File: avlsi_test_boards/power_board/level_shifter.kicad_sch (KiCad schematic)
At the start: 7 parts, among them U19 SN74LVC16T245DLR

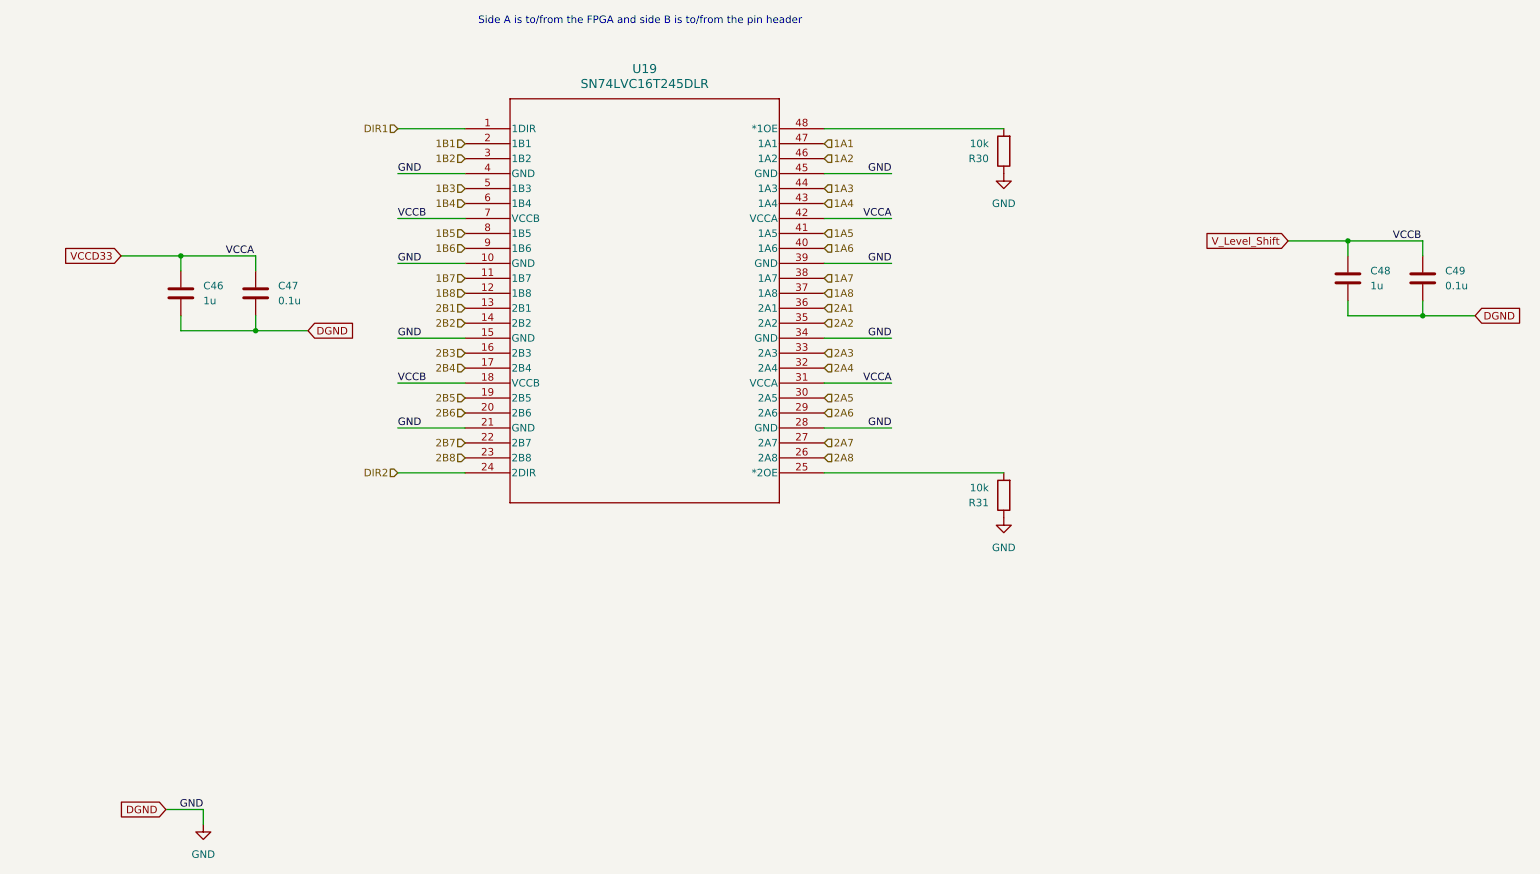
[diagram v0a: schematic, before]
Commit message: Add updated power board layout and schematic
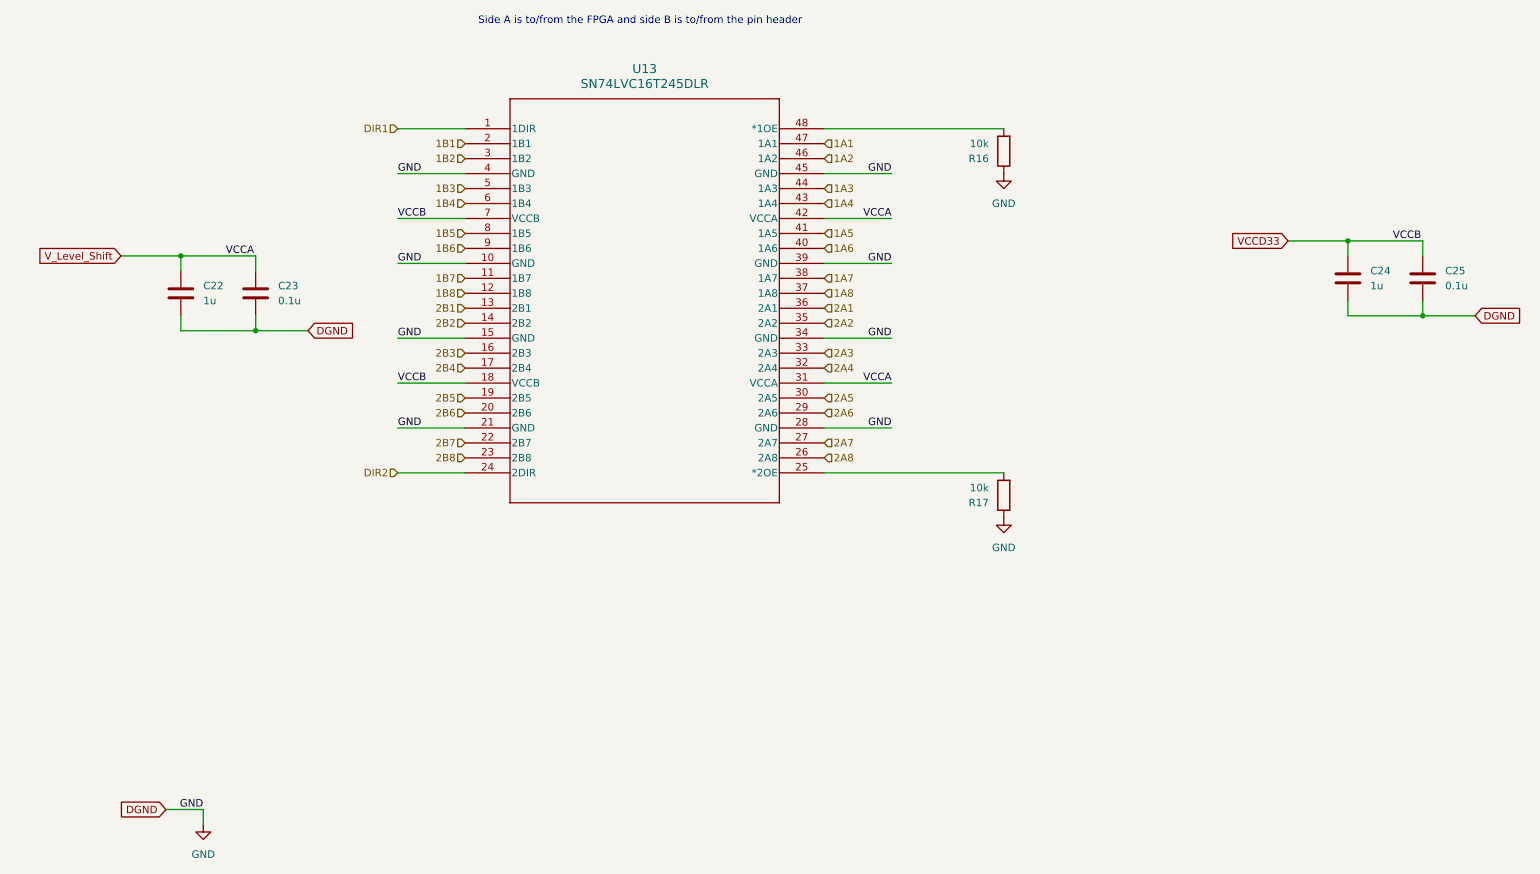
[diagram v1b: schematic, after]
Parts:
- renumbered C46 to C22, C47 to C23, C48 to C24, C49 to C25, R30 to R16, R31 to R17, U19 to U13
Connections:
- net VCCD33: now also C24.1, C25.1, U13.18 (VCCB), U13.7 (VCCB); no longer C22.1, C23.1, U13.31 (VCCA), U13.42 (VCCA)
- net V_Level_Shift: now also C22.1, C23.1, U13.31 (VCCA), U13.42 (VCCA); no longer C24.1, C25.1, U13.18 (VCCB), U13.7 (VCCB)
